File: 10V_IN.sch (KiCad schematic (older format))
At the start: 5 parts, among them U3 LM321

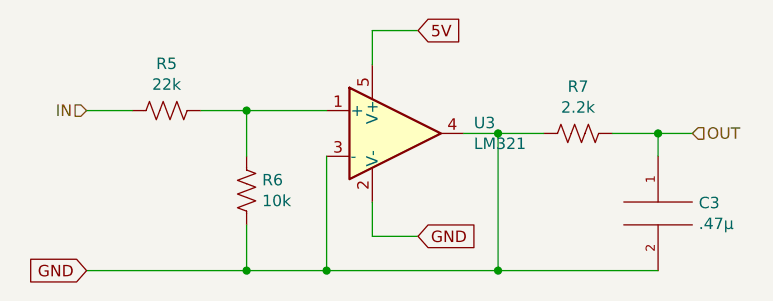
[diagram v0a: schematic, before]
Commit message: Added PWM to 20mA Output Subcircuit
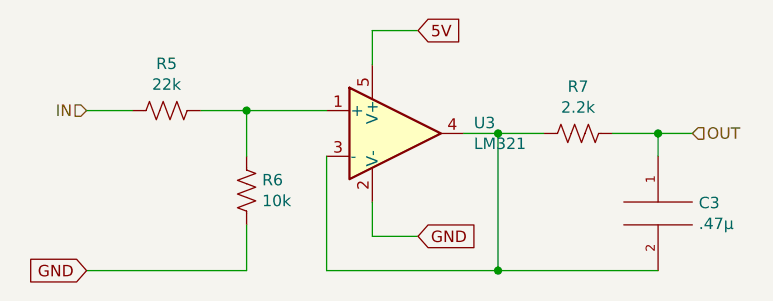
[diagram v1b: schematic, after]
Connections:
- net GND: no longer C3.2, R7.2, U3.3 (-), U3.4
- new net: C3.2, R7.2, U3.3 (-), U3.4
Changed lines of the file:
@@
 $Descr A4 11693 8268
 encoding utf-8
-Sheet 3 3
+Sheet 3 4
 Title "10V to 3.3V Input"
 Date "2021-05-20"
@@
 	5050 3600 5400 3600
 Connection ~ 5050 3600
-Wire Wire Line
-	5050 4300 5400 4300
-Connection ~ 5050 4300
-Connection ~ 5400 4300
 $Comp
 L Device:R_US R?
